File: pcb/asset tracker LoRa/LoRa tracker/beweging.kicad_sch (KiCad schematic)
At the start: 3 parts, among them U3 LIS3DH

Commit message: klaar
print hertekend naar stm32L5
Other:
- note added: "slave addres read = 33 hex slave addres write =32 hex"
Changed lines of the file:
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@@
     (stroke (width 0) (type solid) (color 0 0 0 0))
+  )
+  (text "slave addres read = 33 hex\nslave addres write =32 hex"
+    (at 154.94 95.25 0)
+    (effects (font (size 1.27 1.27)) (justify right bottom))
   )
   (hierarchical_label "LIS_INT1" (shape output) (at 83.82 81.28 180)

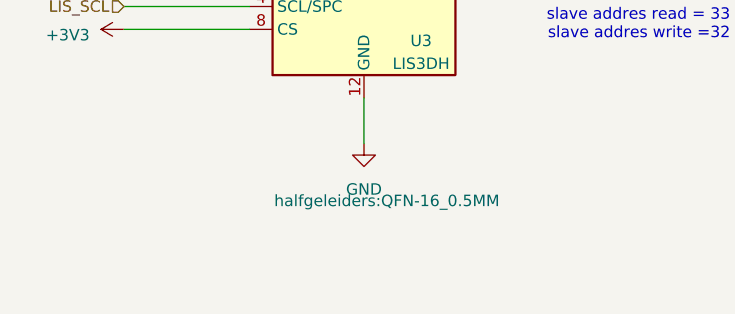
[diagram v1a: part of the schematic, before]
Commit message: versie2
aan versie 2 begonnen met tekenen en code beginnen schrijven voor quadkey
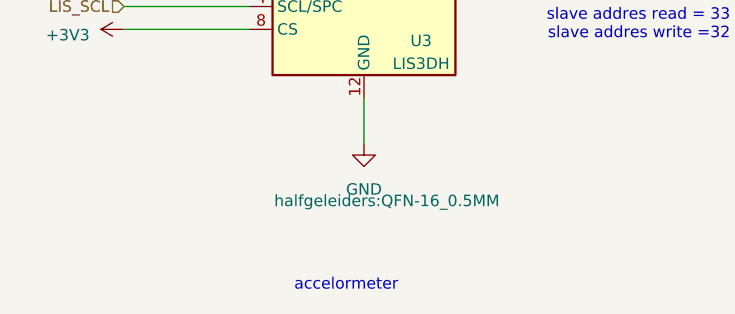
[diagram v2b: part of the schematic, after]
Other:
- note added: "accelormeter"
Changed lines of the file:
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@@
     (stroke (width 0) (type solid) (color 0 0 0 0))
+  )
+  (text "accelormeter\n" (at 114.3 123.19 180)
+    (effects (font (size 1.27 1.27)) (justify right bottom))
   )
   (text "slave addres read = 33 hex\nslave addres write =32 hex"
